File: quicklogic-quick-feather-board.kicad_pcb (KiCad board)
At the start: 6 copper layers, 50.8 x 22.9 mm, 79 parts, among them IC1 EOS-S3, J1 SHF-105-01-L-D-SM, J2 1x12_pinhead, J3 1x16_pinhead, J5 0473460001, Q1 BSS138AKA, Q2 BSS84, U1 TPS62821DLCR, U2 MCP73831T-2ACI_OT, U3 GD25Q16CWIGR, U4 DPS310, U5 MC3635, X1 ECS-_327-12_5-34B-TR

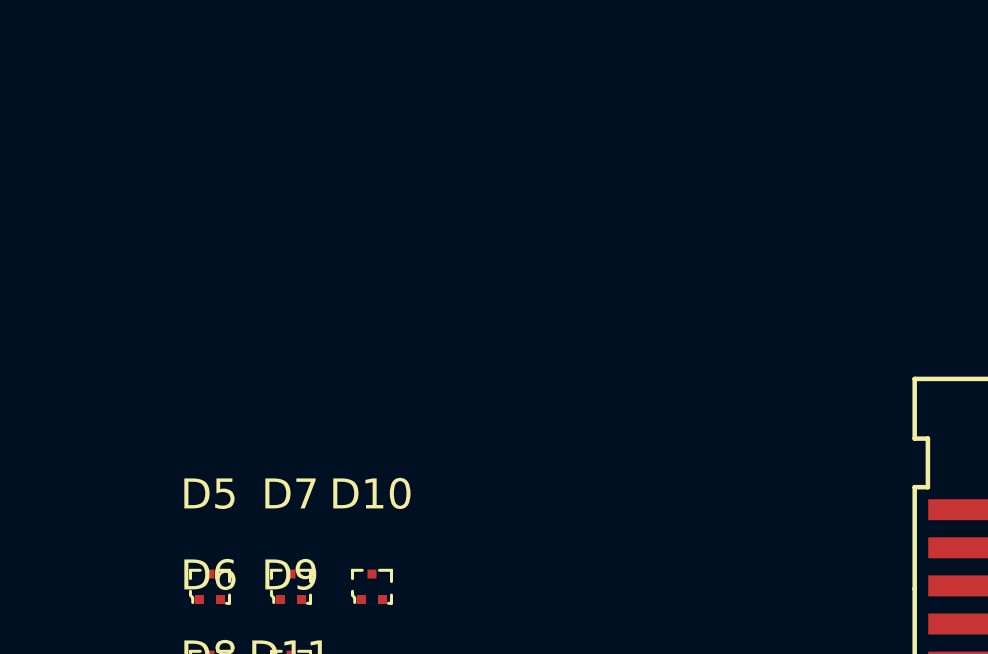
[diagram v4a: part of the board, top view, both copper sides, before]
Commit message: Changes to header, tweaks to LED, added BAT connector
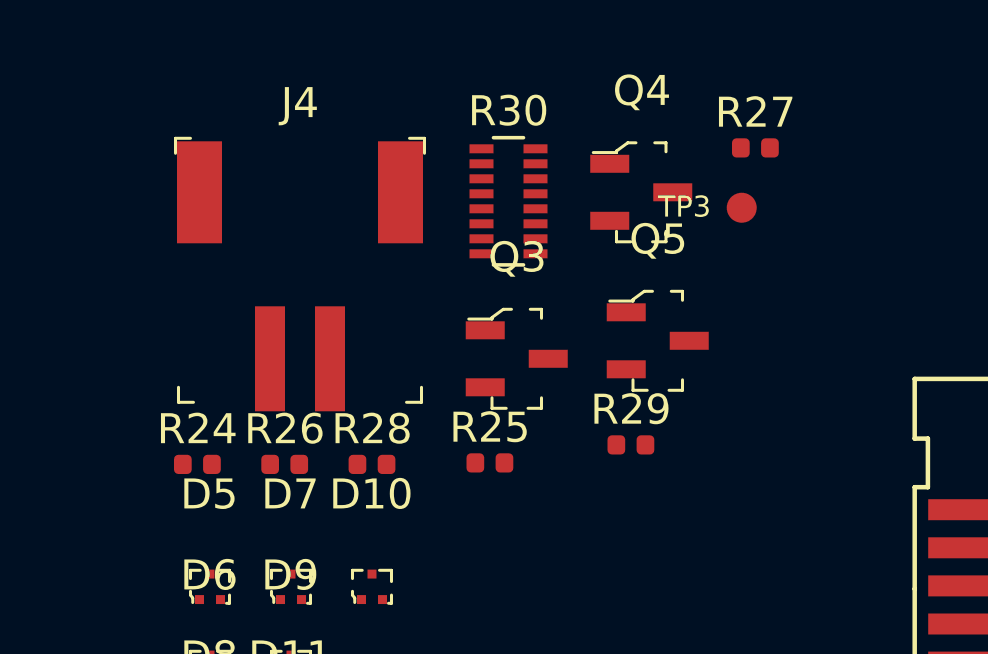
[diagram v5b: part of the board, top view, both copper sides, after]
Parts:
- added J4: S2B-PH-SM4-TB_LF__SN_, antmicro-footprints:PinHeader_2x1mm_P2mm_SMD_RA, F.Cu at (123.0, 71.6)
- added Q3: BSS138AKA, quicklogic-quick-feather-board-footprints:SOT-23-3, F.Cu at (130.2, 71.6)
- added Q4: BSS138AKA, quicklogic-quick-feather-board-footprints:SOT-23-3, F.Cu at (134.4, 66.0)
- added Q5: BSS138AKA, quicklogic-quick-feather-board-footprints:SOT-23-3, F.Cu at (134.9, 71.0)
- added R24: R_100R_0402, quicklogic-quick-feather-board-footprints:0402-res, F.Cu at (119.6, 75.1)
- added R25: R_100R_0402, quicklogic-quick-feather-board-footprints:0402-res, F.Cu at (129.3, 75.1)
- added R26: R_100R_0402, quicklogic-quick-feather-board-footprints:0402-res, F.Cu at (122.5, 75.1)
- added R27: R_22R_0402, quicklogic-quick-feather-board-footprints:0402-res, F.Cu at (138.2, 64.6)
- added R28: R_22R_0402, quicklogic-quick-feather-board-footprints:0402-res, F.Cu at (125.4, 75.1)
- added R29: R_22R_0402, quicklogic-quick-feather-board-footprints:0402-res, F.Cu at (134.0, 74.5)
- added R30: EXB2HV220JV, quicklogic-quick-feather-board-footprints:R_Array_Convex_8x0602, F.Cu at (129.9, 66.3)
- added TP3: TP_SMD1MM, quicklogic-quick-feather-board-footprints:Testpoint_smd_1mm, F.Cu at (137.7, 66.6)
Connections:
- net /HEADER_A0 renamed Net-(J3-Pad5)
- net /HEADER_A1 renamed Net-(J3-Pad6)
- net /HEADER_A2 renamed Net-(J3-Pad7)
- net /HEADER_A3 renamed Net-(J3-Pad8)
- net /HEADER_A4 renamed Net-(J3-Pad9)
- net /HEADER_AREF renamed Net-(J3-Pad3)
- net /HEADER_En renamed Net-(J2-Pad11)
- net /HEADER_P10 renamed Net-(J2-Pad8)
- net /HEADER_P11 renamed Net-(J2-Pad9)
- net /HEADER_P8 renamed Net-(J2-Pad6)
- net /HEADER_P9 renamed Net-(J2-Pad7)
- net /HEADER_USB renamed Net-(J2-Pad10)
- IC1 pad A6: /HEADER_P5 -> /USR_BUTTON
- IC1 pad D2: /LED_R -> /Q_LED_R
- IC1 pad D3: /LED_G -> /Q_LED_G
- IC1 pad E7: /USR_BUTTON -> /HEADER_TX
- IC1 pad F4: /LED_B -> /Q_LED_B
- IC1 pad F7: /HEADER_P7 -> /HEADER_RX
- J2 pad 1: /I2C_SDA -> Net-(J2-Pad1)
- J2 pad 2: /I2C_SCL -> Net-(J2-Pad2)
- J2 pad 3: /HEADER_P5 -> Net-(J2-Pad3)
- J2 pad 4: /HEADER_P6 -> Net-(J2-Pad4)
- J2 pad 5: /HEADER_P7 -> Net-(J2-Pad5)
- J3 pad 10: /HEADER_A5 -> Net-(J3-Pad10)
- J3 pad 11: /HEADER_SCK -> Net-(J3-Pad11)
- J3 pad 12: /HEADER_MOSI -> Net-(J3-Pad12)
- J3 pad 13: /HEADER_MISO -> Net-(J3-Pad13)
- J3 pad 14: /HEADER_RX -> Net-(J3-Pad14)
- J3 pad 15: /HEADER_TX -> Net-(J3-Pad15)
- TP7 pad 1: /HEADER_P7 -> /HEADER_RX
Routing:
- net /Q_LED_R: track 0.00 -> 2.92 mm, vias 0 -> 1
- net /LED_R: track 2.92 -> 0.00 mm, vias 1 -> 0
- net /HEADER_TX: track 0.00 -> 2.09 mm
- net /HEADER_P7: track 2.08 -> 0.00 mm
- net /HEADER_P5: track 1.90 -> 0.00 mm
- net /Q_LED_B: track 0.00 -> 1.75 mm
- net /LED_B: track 1.75 -> 0.00 mm
- net /Q_LED_G: track 0.00 -> 1.50 mm, vias 0 -> 3
- net /LED_G: track 1.50 -> 0.00 mm, vias 3 -> 0
- net Net-(J3-Pad10): track 0.00 -> 1.02 mm
- net /HEADER_A5: track 2.86 -> 1.84 mm
- net Net-(J3-Pad14): track 0.00 -> 0.89 mm
- net Net-(J2-Pad2): track 0.00 -> 0.76 mm
- net /I2C_SCL: track 2.57 -> 1.81 mm
- net Net-(J3-Pad11): track 0.00 -> 0.76 mm
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
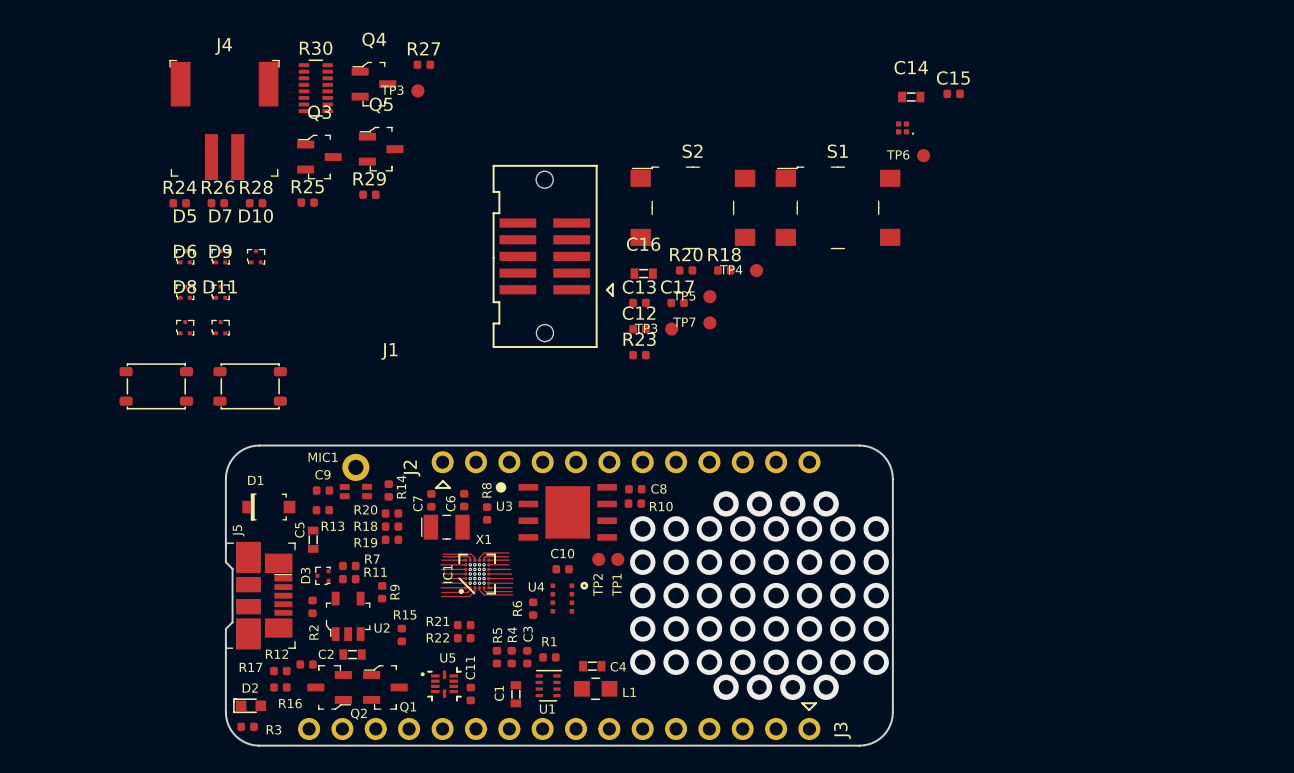
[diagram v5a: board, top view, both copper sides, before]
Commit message: Added TBDs to schematics
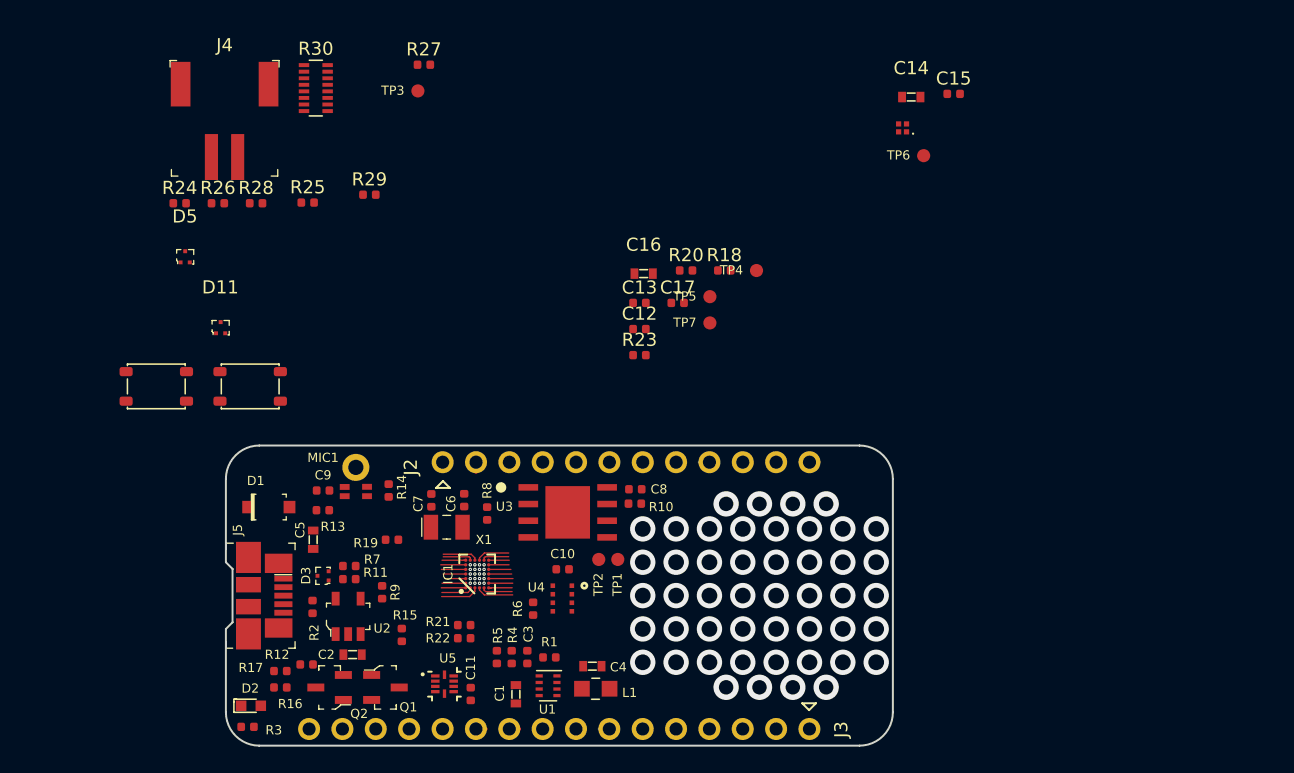
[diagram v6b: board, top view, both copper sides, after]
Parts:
- removed D10, D6, D7, D8, D9: TPD2EUSB30DRTR, quicklogic-quick-feather-board-footprints:SOT-3
- removed J1: SHF-105-01-L-D-SM, quicklogic-quick-feather-board-footprints:SHF-105-01-L-D-SM
- removed Q3, Q4, Q5: BSS138AKA, quicklogic-quick-feather-board-footprints:SOT-23-3
- removed the R18 at (135.8, 99.8)
- removed the R20 at (135.8, 98.8)
- removed the S1 at (169.7, 75.5)
- removed the S2 at (158.7, 75.5)
- removed the TP3 at (157.1, 84.8)
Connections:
- IC1 pad B4: /SDW_IO -> /SWD_IO
- R24 pad 2: Net-(Q3-Pad3) -> /Q_LED_B
- R25 pad 2: Net-(Q4-Pad3) -> /Q_LED_G
- R26 pad 2: Net-(Q5-Pad3) -> /Q_LED_R
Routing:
- net /SWD_IO: track 0.00 -> 2.37 mm, vias 0 -> 1
- net /SDW_IO: track 2.37 -> 0.00 mm, vias 1 -> 0

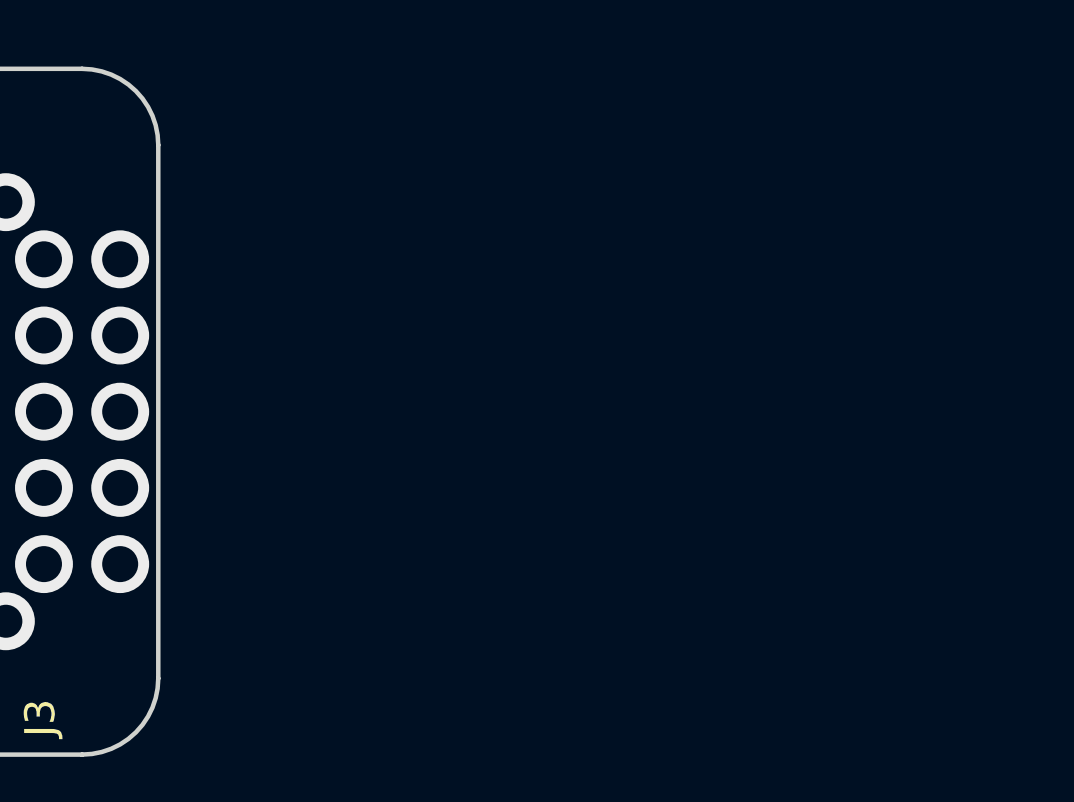
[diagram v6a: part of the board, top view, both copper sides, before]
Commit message: Added pinhead connectors for debug and programming
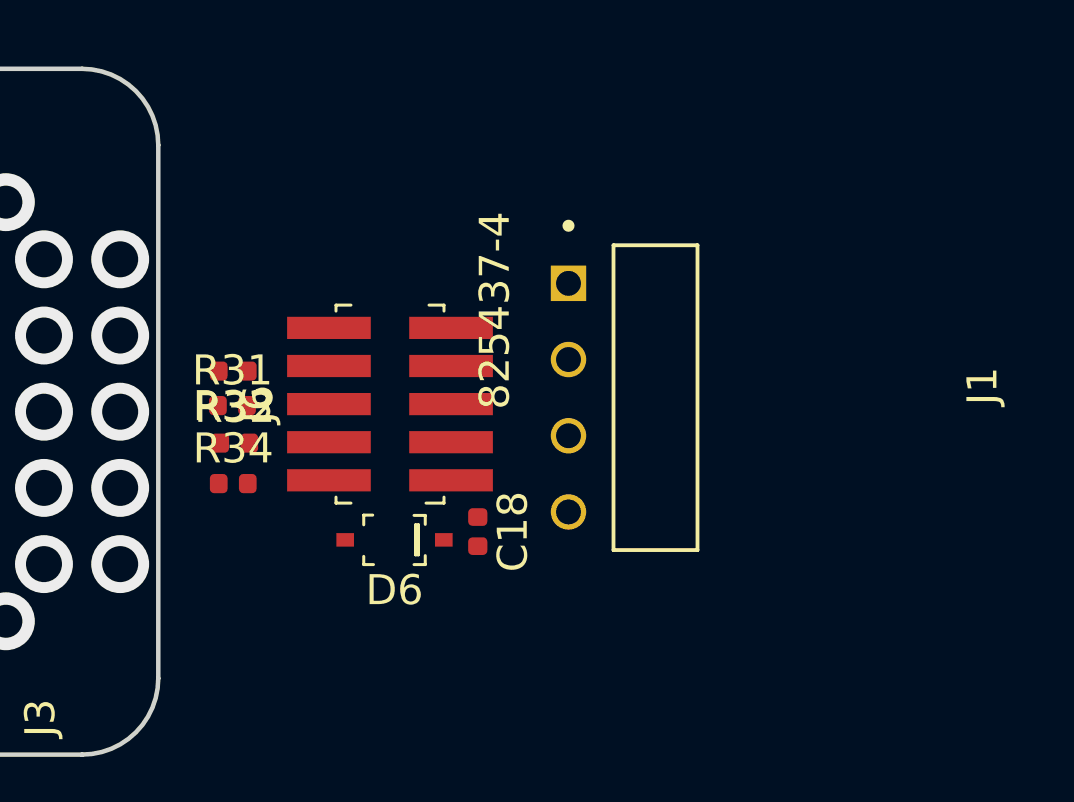
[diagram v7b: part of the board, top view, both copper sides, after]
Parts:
- added C18: C_100n_0402_6V3, quicklogic-quick-feather-board-footprints:0402-cap, F.Cu at (184.6, 109.0)
- added D6: SD05C.TCT, quicklogic-quick-feather-board-footprints:SOD-323, F.Cu at (181.8, 109.3)
- added J1: 825437-4, quicklogic-quick-feather-board-footprints:TE_825437-4, F.Cu at (187.6, 100.7)
- added J6: FTSH-105-01-L-DV-K, quicklogic-quick-feather-board-footprints:PinHeader_2x5_P1.27_SMD, F.Cu at (181.6, 104.8)
- added R31: R_10k_0402, quicklogic-quick-feather-board-footprints:0402-res, F.Cu at (176.4, 104.8)
- added R32: R_10k_0402, quicklogic-quick-feather-board-footprints:0402-res, F.Cu at (176.4, 106.0)
- added R33: R_0R_0402, quicklogic-quick-feather-board-footprints:0402-res, F.Cu at (176.4, 103.7)
- added R34: R_10k_0402, quicklogic-quick-feather-board-footprints:0402-res, F.Cu at (176.4, 107.4)
- C12, C13, C15, C17: footprint antmicro-footprints:0402-cap -> quicklogic-quick-feather-board-footprints:0402-cap
- J4: footprint antmicro-footprints:PinHeader_2x1mm_P2mm_SMD_RA -> quicklogic-quick-feather-board-footprints:PinHeader_2x1mm_P2mm_SMD_RA

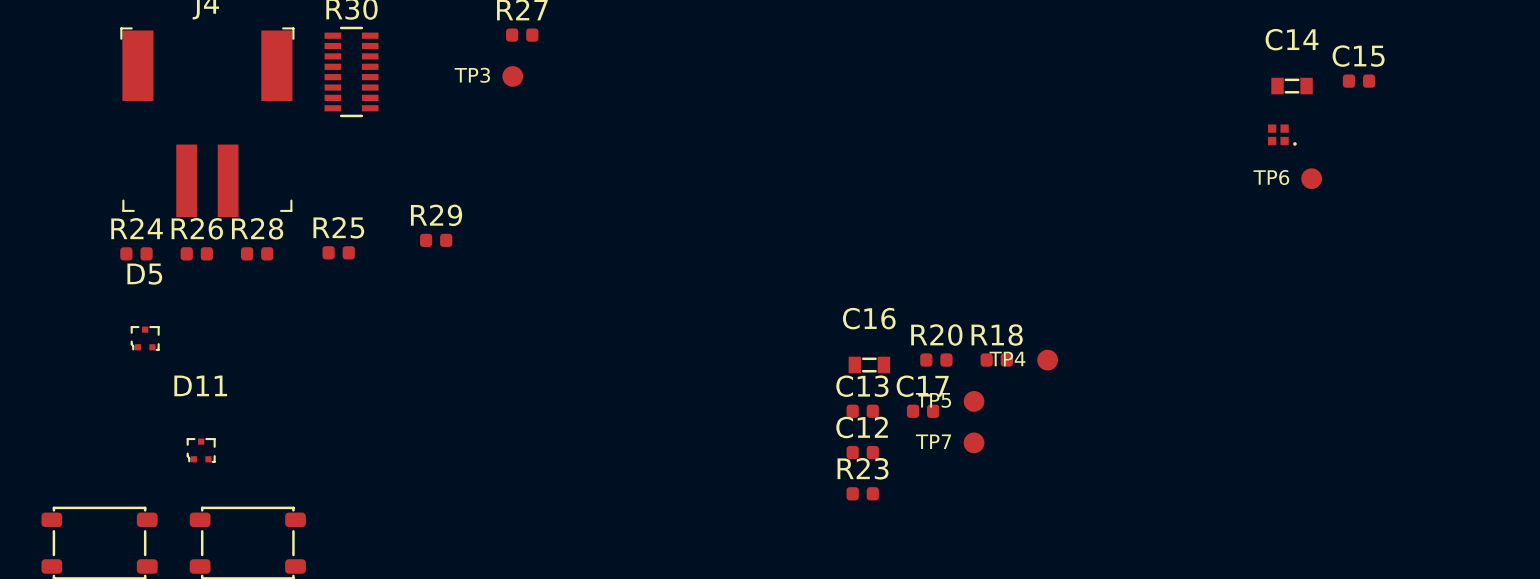
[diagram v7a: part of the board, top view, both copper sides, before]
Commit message: Added LED driving transistors
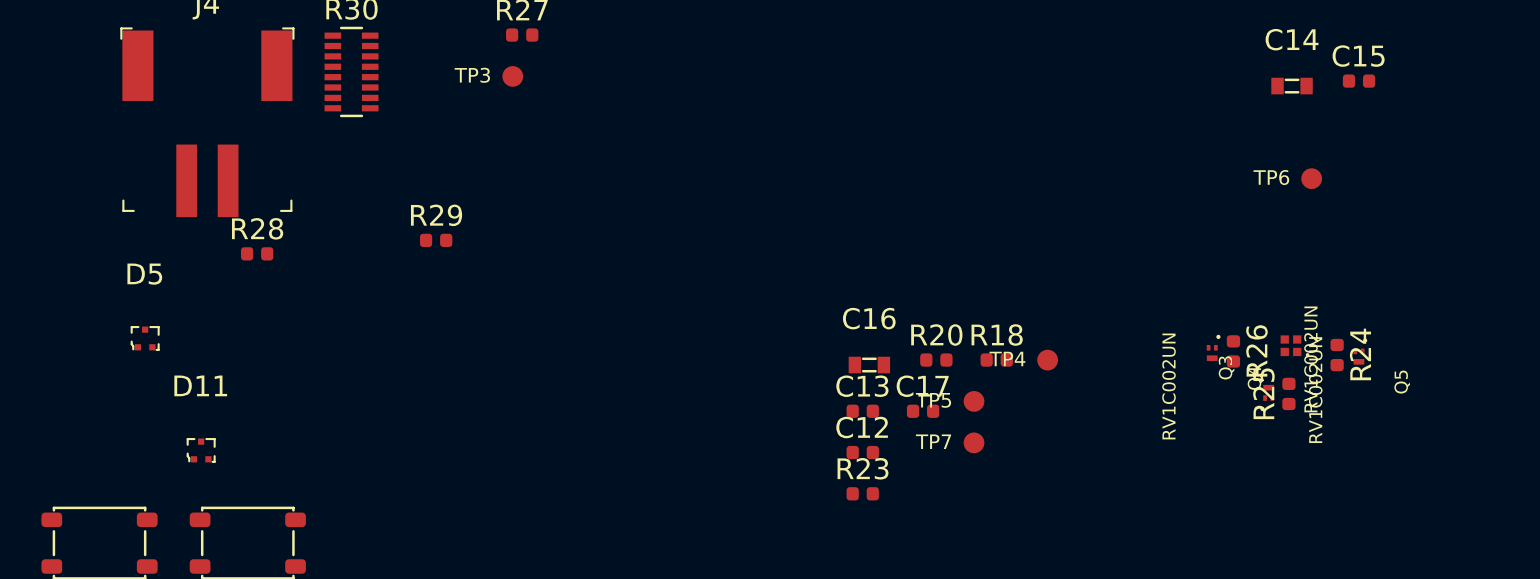
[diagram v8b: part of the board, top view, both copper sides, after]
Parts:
- added Q3: RV1C002UN, quicklogic-quick-feather-board-footprints:VML0806, F.Cu at (174.2, 81.9)
- added Q4: RV1C002UN, quicklogic-quick-feather-board-footprints:VML0806, F.Cu at (171.4, 79.8)
- added Q5: RV1C002UN, quicklogic-quick-feather-board-footprints:VML0806, F.Cu at (178.5, 80.0)
- R25: value R_100R_0402 -> R_220R_0402
- moved R24 58.1 mm to (177.5, 80.0), turned to 270 degrees
- moved R26 50.2 mm to (172.5, 79.8), turned to 270 degrees
- moved R25 46.3 mm to (175.2, 81.9), turned to 90 degrees
- moved D4 10.2 mm to (175.2, 79.5)
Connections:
- R24 pad 2: /Q_LED_B -> Net-(Q5-Pad3)
- R25 pad 1: /LED_G -> /LED_R
- R25 pad 2: /Q_LED_G -> Net-(Q3-Pad3)
- R26 pad 1: /LED_R -> /LED_G
- R26 pad 2: /Q_LED_R -> Net-(Q4-Pad3)
